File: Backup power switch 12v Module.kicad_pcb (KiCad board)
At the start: 2 copper layers, 94.3 x 82.4 mm, 56 parts, among them J1 BAT IN, J2 PWR IN, J3 LOAD PWR OUT, J5 Conn_01x06, K1 SANYOU_SRD_Form_C, Q2 AO3401A, Q3 BC817, U1 LM393, U2 INA219AxD, U3 INA219AxD, U4 LTV-817, U5 LTV-817, U6 CN3763, U7 ESP32-C3 Pro Mini, U8 AMS1117-3.3

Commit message: DRC check
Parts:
- D7: footprint Package_TO_SOT_THT:TO-247-3_Vertical -> PCM_Package_TO_SOT_THT_AKL_OneLayer:TO-220-3_Staggered_Vertical
- J5: value Conn_01x06 -> Esternal; footprint Connector_JST:JST_PH_S6B-PH-K_1x06_P2.00mm_Horizontal -> Connector_JST:JST_PH_B8B-PH-K_1x08_P2.00mm_Vertical
- K1: value SANYOU_SRD_Form_C -> SRD-12VDC-SL-C
- L2: footprint Inductor_SMD:L_TDK_VLS6045EX_VLS6045AF -> Inductor_SMD:L_TechFuse_SL0624
- U1: footprint Package_SO:SOP-8_3.76x4.96mm_P1.27mm -> Package_DIP:DIP-8_W7.62mm
- moved C5 28.6 mm to (151.1, 111.7)
- moved U1 8.82 mm to (161.7, 112.8)
- moved D7 5.27 mm to (178.9, 87.1)
- moved TP1 4.52 mm to (179.4, 115.8)
- moved TP2 4.52 mm to (179.4, 122.7)
- moved TP3 4.52 mm to (179.4, 109.0)
- moved U4 3.21 mm to (132.9, 105.4)
- moved U5 3.21 mm to (132.9, 113.0)
- moved D3 2.37 mm to (166.3, 120.7)
- moved R10 2.37 mm to (165.7, 101.1)
- moved R11 2.37 mm to (165.7, 103.9)
- moved R13 2.37 mm to (165.7, 106.4)
- moved R2 2.37 mm to (165.7, 111.5)
- moved R3 2.37 mm to (165.7, 109.0)
- moved C1 1.80 mm to (130.6, 126.5), turned to 0 degrees
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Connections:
- U7 pad 0: unconnected-(U7-GPIO0/A0-Pad0) -> Net-(J5-Pin_8)
- U7 pad 1: unconnected-(U7-GPIO1/A1-Pad1) -> Net-(J5-Pin_7)
- U8 pad 4: GNDPWR -> unconnected-(U8-Heat-Pad4)
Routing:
- net Net-(J5-Pin_7): track 0.00 -> 31.6 mm
- net Net-(J5-Pin_8): track 0.00 -> 28.8 mm
- net GNDPWR: track 338.2 -> 348.5 mm, vias 5 -> 4
- net Net-(R3-Pad2): track 71.8 -> 78.7 mm
- net Net-(Q3-B): track 21.8 -> 15.9 mm
- net BAT OUT 12 +: track 102.6 -> 97.3 mm
- net BAT IN 12 +: track 115.0 -> 110.3 mm
- net /Batary Charger module/CHRG: track 41.4 -> 45.6 mm
- net /Batary Charger module/DONE: track 40.2 -> 44.3 mm
- net Net-(R2-Pad2): track 101.5 -> 105.4 mm
- net Net-(D6-A): track 12.7 -> 8.79 mm
- net +3V3: track 135.7 -> 132.1 mm
- net Net-(D3-A): track 24.2 -> 20.9 mm
- net Net-(U1A--): track 6.80 -> 3.48 mm
- net Net-(R1-Pad2): track 13.5 -> 16.7 mm
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- added copper zone on F.Cu, net unconnected-(U8-Heat-Pad4)
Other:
- board text added: "A0"
- board text added: "A1"
- board text removed: "To BAT Load"
- board text removed: "To Battary"
- board text removed: "To PWR load"

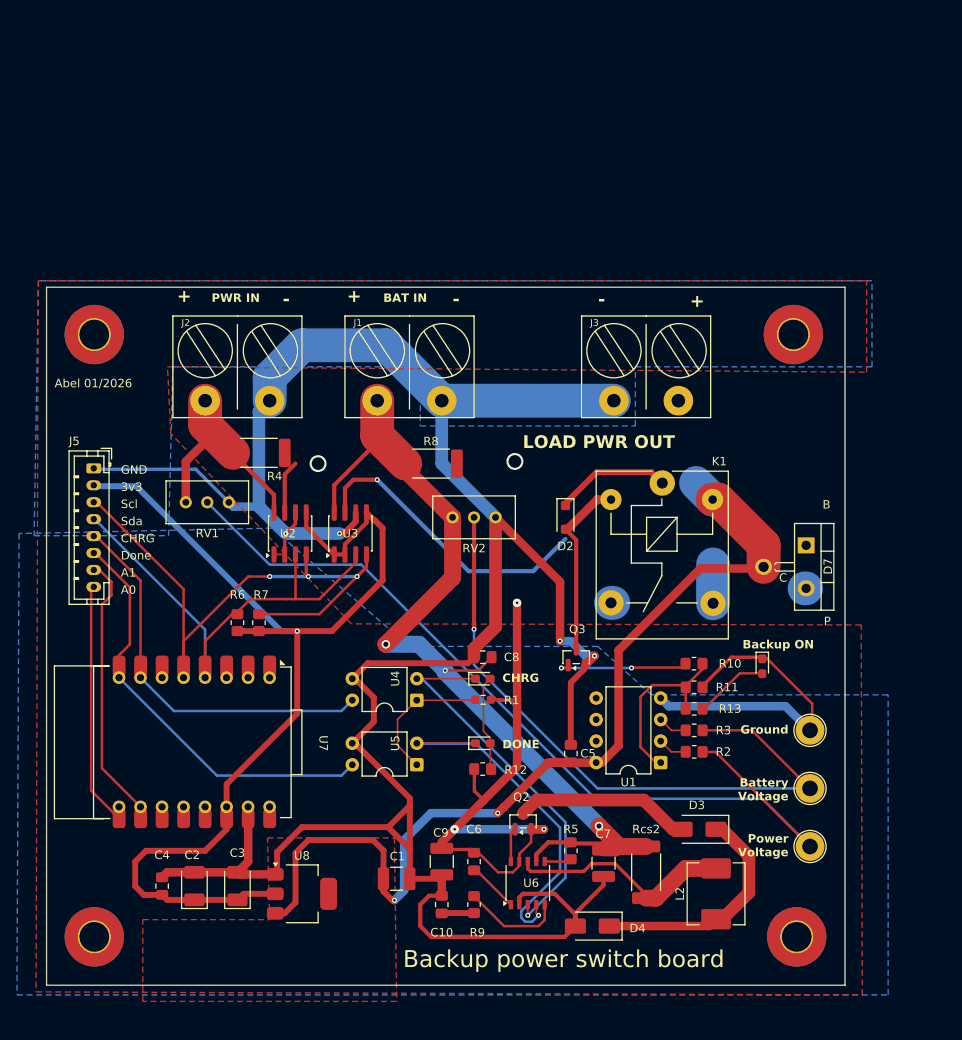
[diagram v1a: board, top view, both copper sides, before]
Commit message: Add bat input stabilizer
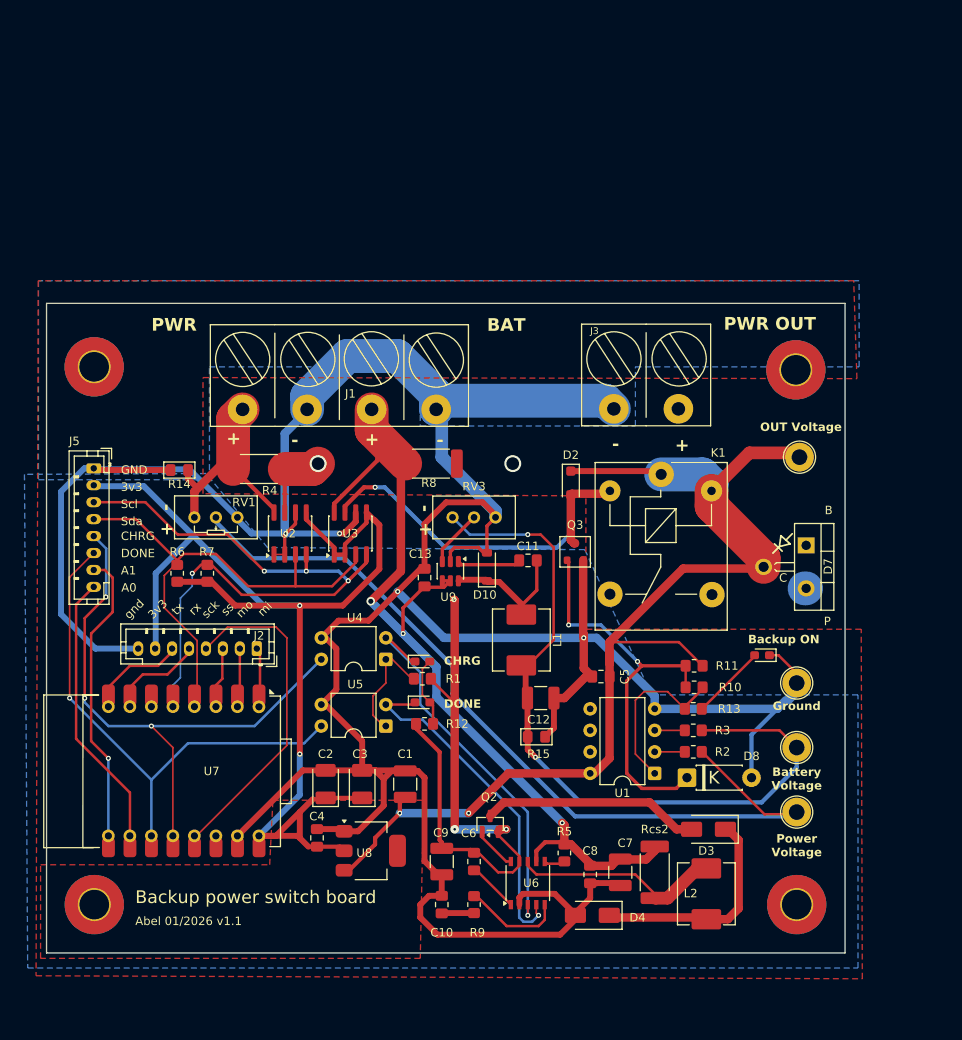
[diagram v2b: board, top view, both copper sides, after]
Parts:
- removed RV2: 10k, Potentiometer_THT:Potentiometer_Bourns_3296W_Vertical
- added C11: 2.2uF, Capacitor_SMD:C_0805_2012Metric_Pad1.18x1.45mm_HandSolder, F.Cu at (146.1, 88.9)
- added C12: 22uF, Capacitor_SMD:C_1210_3225Metric_Pad1.33x2.70mm_HandSolder, F.Cu at (147.6, 105.2)
- added C13: 2.2uF, Capacitor_SMD:C_0805_2012Metric_Pad1.18x1.45mm_HandSolder, F.Cu at (133.9, 90.9)
- added D10: 1N5819, Diode_SMD:D_SOD-123, F.Cu at (141.2, 89.7)
- added D8: 1N4744A, Diode_THT:D_DO-41_SOD81_P7.62mm_Horizontal, F.Cu at (164.8, 114.6)
- added L1: 47uH, Inductor_SMD:L_TechFuse_SL0650, F.Cu at (145.3, 98.3)
- added R14: 10k, PCM_Resistor_SMD_AKL:R_0805_2012Metric_Pad1.15x1.40mm_HandSolder, F.Cu at (104.9, 78.2)
- added R15: 10k, PCM_Resistor_SMD_AKL:R_0805_2012Metric_Pad1.15x1.40mm_HandSolder, F.Cu at (147.1, 109.7)
- added RV3: 10k, Potentiometer_THT:Potentiometer_Bourns_3296W_Vertical, F.Cu at (142.2, 83.8)
- added TP4: OUT, TestPoint:TestPoint_Loop_D2.50mm_Drill1.85mm, F.Cu at (178.1, 76.7)
- added U9: LMR14203, Package_TO_SOT_SMD:SOT-23-6, F.Cu at (136.9, 90.2)
- D6: value Switch -> LED
- D7: value MBRF20100CT -> MURF2060CT
- J1: footprint TerminalBlock_Local:ScrewTerminal_KF7.62_2P -> TerminalBlock_Local:ScrewTerminal_KF7.62_4P
- J2: value PWR IN -> Esternal; footprint TerminalBlock_Local:ScrewTerminal_KF7.62_2P -> Connector_JST:JST_PH_B8B-PH-K_1x08_P2.00mm_Vertical
- J3: value LOAD PWR OUT -> PWR OUT
- Q3: value BC817 -> BSS138; footprint Package_TO_SOT_SMD:SOT-23 -> PCM_Package_TO_SOT_SMD_AKL:SOT-23
- R1: footprint Resistor_SMD:R_0603_1608Metric_Pad0.98x0.95mm_HandSolder -> Resistor_SMD:R_0805_2012Metric_Pad1.20x1.40mm_HandSolder
- R11: value 10K -> 10k
- RV1: footprint Potentiometer_THT:Potentiometer_Bourns_3296W_Vertical -> PCM_Potentiometer_THT_AKL:Potentiometer_Bourns_3296W_Vertical
- moved J2 33.4 mm to (114.0, 99.3), turned to 180 degrees
- moved C8 28.6 mm to (153.4, 126.0), turned to -90 degrees
- moved C2 19.6 mm to (122.2, 115.3)
- moved C4 19.2 mm to (121.2, 121.7)
- moved C3 19.0 mm to (126.5, 115.3)
- moved Q3 12.4 mm to (151.6, 87.9)
- moved C1 11.2 mm to (131.6, 115.3), turned to 90 degrees
- moved C5 9.76 mm to (154.7, 102.6), turned to 180 degrees
- moved J1 9.69 mm to (123.8, 71.1)
- moved U8 9.58 mm to (127.5, 123.2)
- moved R6 9.19 mm to (104.6, 90.4)
- moved R12 8.69 mm to (133.9, 108.2)
- moved D1 8.61 mm to (133.6, 105.7)
- moved R7 8.43 mm to (108.2, 90.4)
- moved R1 7.58 mm to (133.6, 102.9)
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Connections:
- net Net-(R3-Pad2) renamed /StepDown Convertor/BAT Low 12 +
- J1 pad 1: BAT IN 12 + -> PWR IN 12 +
- J2 pad 1: PWR IN 12 + -> Net-(J2-Pin_1)
- J2 pad 2: GNDPWR -> Net-(J2-Pin_2)
- Q3 pad 1: Net-(Q3-B) -> Net-(D8-K)
- R10 pad 2: Net-(Q3-B) -> Net-(D8-K)
- R11 pad 1: GNDPWR -> COMMON OUT 12 +
- R11 pad 2: SIG -> Net-(D8-K)
- U7 pad 0: Net-(J5-Pin_8) -> Net-(J5-Pin_7)
- U7 pad 1: Net-(J5-Pin_7) -> Net-(J5-Pin_8)
- U7 pad 2: unconnected-(U7-GPIO2/A2-Pad2) -> Net-(J5-Pin_6)
- U7 pad 20: Net-(J5-Pin_5) -> Net-(J2-Pin_5)
- U7 pad 21: Net-(J5-Pin_6) -> Net-(J2-Pin_6)
- U7 pad 3: unconnected-(U7-GPIO3/A3-Pad3) -> Net-(J5-Pin_5)
- U7 pad 4: unconnected-(U7-GPIO4/A4-Pad4) -> Net-(J2-Pin_4)
- U7 pad 5: unconnected-(U7-GPIO5/A5-Pad5) -> Net-(J2-Pin_1)
- U7 pad 6: unconnected-(U7-GPIO6-Pad6) -> Net-(J2-Pin_2)
- U7 pad 7: unconnected-(U7-GPIO7-Pad7) -> Net-(J2-Pin_3)
- U7 pad P3: +3V3 -> unconnected-(U7-VCC_3V-PadP3)
- U7 pad P5: unconnected-(U7-VCC_5V-PadP5) -> +3V3
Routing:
- net GNDPWR: track 348.5 -> 418.8 mm
- net Net-(D8-K): track 0.00 -> 47.9 mm, vias 0 -> 2
- net Net-(J2-Pin_4): track 0.00 -> 39.7 mm
- net +3V3: track 132.1 -> 153.9 mm, vias 1 -> 2
- net Net-(J5-Pin_5): track 46.3 -> 68.0 mm, vias 0 -> 3
- net Net-(D10-K): track 0.00 -> 17.0 mm
- net Net-(Q3-B): track 15.9 -> 0.00 mm, vias 2 -> 0
- net Net-(J2-Pin_6): track 0.00 -> 11.9 mm
- net Net-(J5-Pin_6): track 50.0 -> 61.6 mm, vias 0 -> 1
- net /StepDown Convertor/BAT Low 12 +: track 78.7 -> 90.1 mm, vias 1 -> 2
- net Net-(D2-A): track 21.5 -> 10.8 mm
- net BAT OUT 12 +: track 97.3 -> 86.9 mm
- net Net-(J2-Pin_5): track 0.00 -> 10.1 mm
- net Net-(U9-CB): track 0.00 -> 7.54 mm
- net Net-(J2-Pin_3): track 0.00 -> 7.20 mm
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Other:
- board size 94.3 x 82.4 mm -> 94.3 x 76.7 mm
- board text added: "Abel 01/2026 v1.1"
- board text added: "BAT"
- board text added: "OUT Voltage"
- board text added: "PWR"
- board text added: "gnd"
- board text added: "mi"
- board text added: "mo"
- board text added: "rx"
- board text added: "sck"
- board text added: "ss"
- board text added: "tx"
- board text removed: "Abel 01/2026"
- board text removed: "Done"

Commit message: Fix comparator out signal pullup
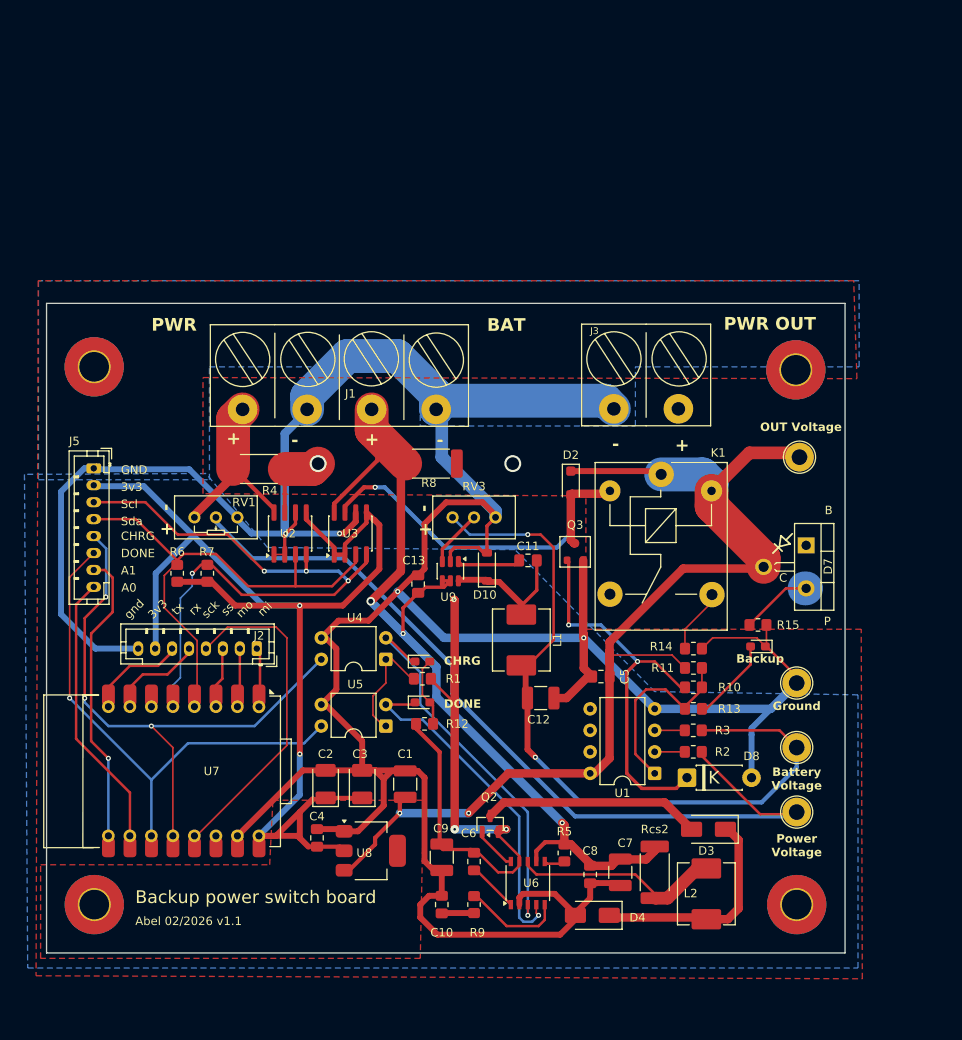
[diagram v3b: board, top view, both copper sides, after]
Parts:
- J2: value Esternal -> External
- R14, R15: footprint PCM_Resistor_SMD_AKL:R_0805_2012Metric_Pad1.15x1.40mm_HandSolder -> Resistor_SMD:R_0805_2012Metric_Pad1.20x1.40mm_HandSolder
- moved R14 64.3 mm to (165.6, 99.3), turned to 0 degrees
- moved R15 29.3 mm to (173.2, 96.5)
- moved D6 1.14 mm to (173.2, 99.1)
- moved C13 1.08 mm to (133.1, 91.7)
- moved C9 0.51 mm to (135.9, 124.0)
- moved R11 0.27 mm to (165.6, 101.6), turned to 0 degrees
- moved R10 0.08 mm to (165.6, 103.9)
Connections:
- R11 pad 2: Net-(D8-K) -> SIG
- R14 pad 1: PWR IN 12 + -> BAT OUT 12 +
- R15 pad 1: /StepDown Convertor/BAT Low 12 + -> PWR OUT 12 +
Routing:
- net PWR OUT 12 +: track 150.6 -> 159.1 mm
- net BAT OUT 12 +: track 86.9 -> 94.6 mm
- net GNDPWR: track 418.8 -> 415.0 mm
- net COMMON OUT 12 +: track 139.5 -> 137.2 mm
- net PWR IN 12 +: track 32.5 -> 30.4 mm
- net SIG: track 20.5 -> 22.6 mm
- net Net-(D8-K): track 47.9 -> 46.6 mm
- net Net-(D6-A): track 8.93 -> 10.1 mm
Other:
- board text added: "Abel 02/2026 v1.1"
- board text added: "Backup"
- board text removed: "Abel 01/2026 v1.1"
- board text removed: "Backup ON"

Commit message: Add power sockwr
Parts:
- added HS1: Heatsink, Heatsink:Heatsink_Stonecold_HS-S01_13.21x6.35mm, F.Cu at (181.1, 91.4)
- added J4: Barrel_Jack_MountingPin, Connector_BarrelJack:BarrelJack_Horizontal, F.Cu at (175.0, 118.9)
- added J6: Barrel_Jack_MountingPin, Connector_BarrelJack:BarrelJack_Horizontal, F.Cu at (175.0, 78.2)
- added J8: Barrel_Jack_MountingPin, Connector_BarrelJack:BarrelJack_Horizontal, F.Cu at (175.0, 106.2)
- J1: value BAT IN -> BAT/PWR IN
- moved TP3 83.4 mm to (103.5, 65.4)
- moved R14 35.2 mm to (142.9, 72.4), turned to 90 degrees
- moved TP4 34.6 mm to (145.4, 65.4)
- moved J2 32.6 mm to (106.8, 131.1), turned to 0 degrees
- moved R15 30.9 mm to (149.0, 115.6)
- moved R10 17.1 mm to (149.0, 108.0)
- moved R3 17.1 mm to (149.0, 113.0), turned to 180 degrees
- moved R11 17.1 mm to (149.0, 105.4)
- moved R2 16.7 mm to (149.0, 110.5), turned to 180 degrees
- moved TP1 13.8 mm to (165.9, 104.1)
- moved U1 12.9 mm to (153.7, 103.5), turned to 0 degrees
- moved TP2 12.7 mm to (165.9, 114.3)
- moved D3 11.9 mm to (155.6, 119.4)
- moved R13 11.4 mm to (156.8, 99.1)
- moved D6 11.3 mm to (161.9, 99.1)
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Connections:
- net /Batary Charger module/CHRG renamed /Li-Io 3S Batary Charger module/CHRG
- net /Batary Charger module/DONE renamed /Li-Io 3S Batary Charger module/DONE
- net /StepDown Convertor/BAT Low 12 + renamed /Battery voltage level limiter/BAT Low 12 +
- U4 pad 4: Net-(J5-Pin_5) -> Net-(J5-Pin_8)
- U5 pad 4: Net-(J5-Pin_6) -> Net-(J5-Pin_7)
- U7 pad 0: Net-(J5-Pin_7) -> Net-(J5-Pin_5)
- U7 pad 1: Net-(J5-Pin_8) -> Net-(J5-Pin_6)
- U7 pad 2: Net-(J5-Pin_6) -> Net-(J5-Pin_7)
- U7 pad 3: Net-(J5-Pin_5) -> Net-(J5-Pin_8)
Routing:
- net GNDPWR: track 415.0 -> 505.7 mm, vias 4 -> 11
- net COMMON OUT 12 +: track 137.2 -> 184.1 mm
- net Net-(J5-Pin_5): track 68.0 -> 26.1 mm, vias 3 -> 0
- net Net-(J5-Pin_6): track 61.6 -> 23.2 mm, vias 1 -> 0
- net Net-(J5-Pin_4): track 59.2 -> 83.4 mm
- net Net-(J5-Pin_3): track 77.5 -> 99.5 mm, vias 4 -> 5
- net /Battery voltage level limiter/BAT Low 12 +: track 90.1 -> 70.4 mm, vias 2 -> 3
- net BAT OUT 12 +: track 94.6 -> 76.0 mm, vias 2 -> 3
- net Net-(R2-Pad2): track 100.3 -> 82.1 mm, vias 0 -> 1
- net Net-(J2-Pin_2): track 6.98 -> 20.1 mm
- net Net-(J2-Pin_1): track 7.08 -> 20.1 mm
- net Net-(J2-Pin_3): track 7.20 -> 20.2 mm
- net Net-(D3-A): track 25.8 -> 12.9 mm
- net Net-(D3-K): track 26.1 -> 36.9 mm
- net SIG: track 22.6 -> 12.4 mm
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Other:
- board size 94.3 x 76.7 mm -> 94.3 x 76.2 mm
- board text added: "Abel 02/2026 v2.1"
- board text removed: "Abel 02/2026 v1.1"
